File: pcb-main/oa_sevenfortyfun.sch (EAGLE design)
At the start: 46 parts, among them J1 1X01-TERM, J2 1X01-TERM, J3 1X01-TERM, J4 1X01-TERM, J5 1X01-TERM, J6 1X01-TERM, J7 1X01-TERM, J8 1X01-TERM, J9 2X04SHR, Q1 2N3904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

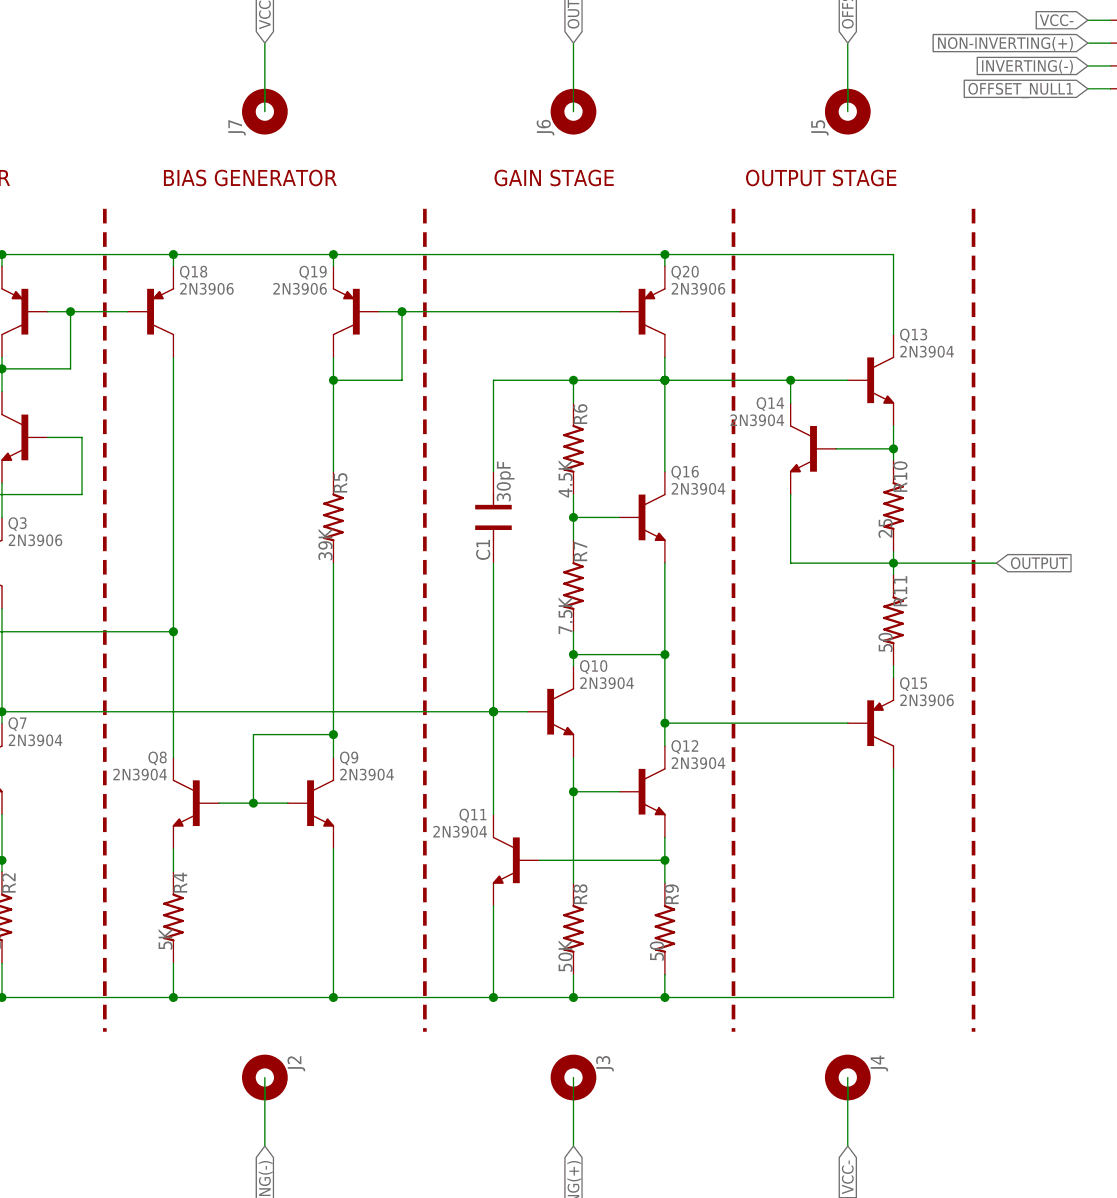
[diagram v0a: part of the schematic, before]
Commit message: matching functional blocks to v1.0
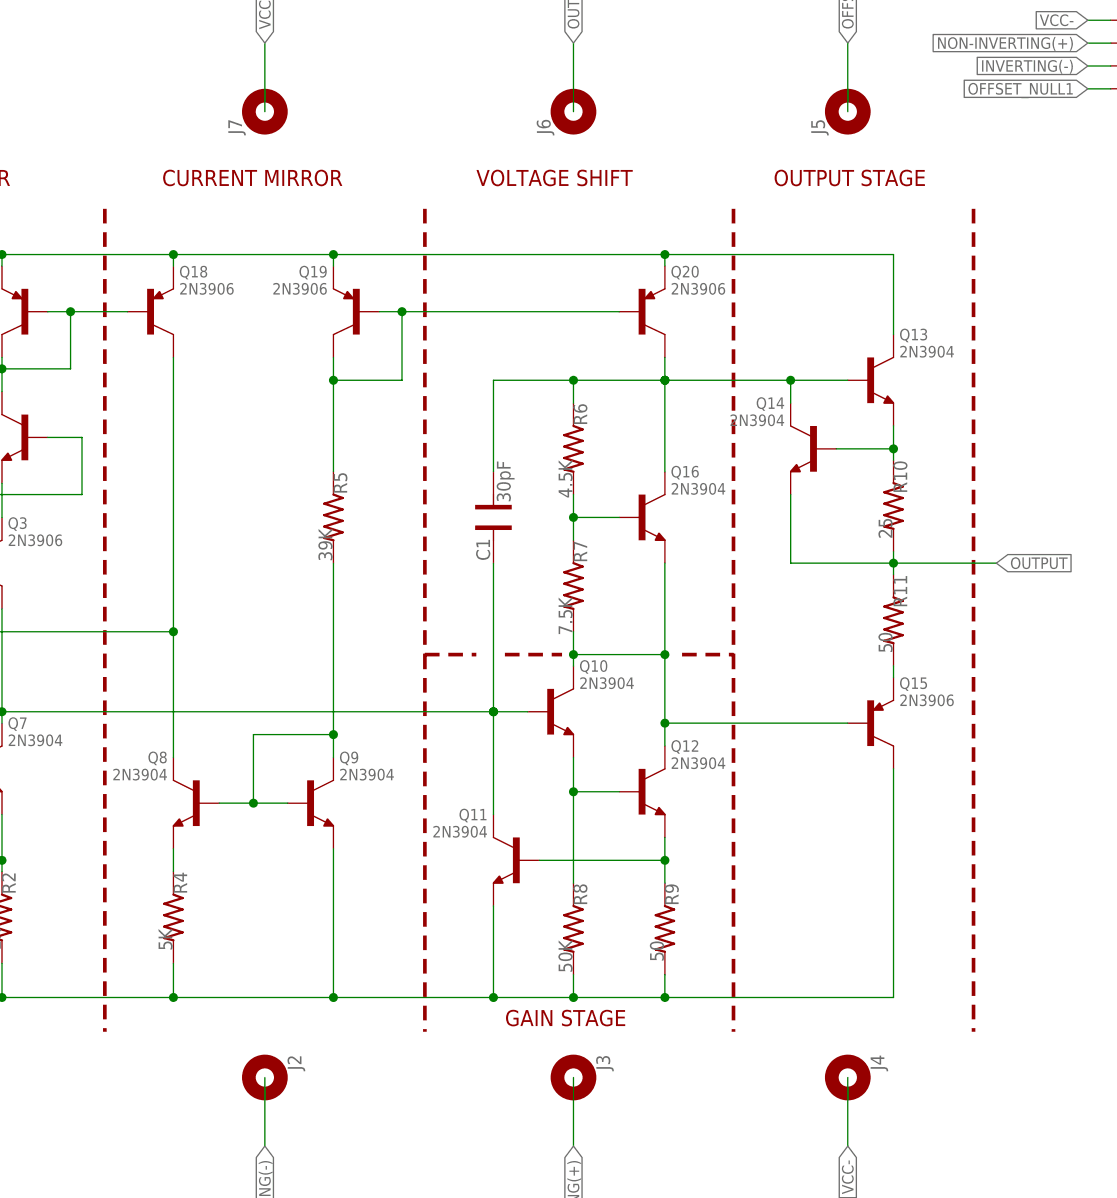
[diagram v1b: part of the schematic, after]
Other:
- note added: "CURRENT MIRROR"
- note added: "VOLTAGE SHIFT"
- note removed: "BIAS GENERATOR"
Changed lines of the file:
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@@
 <plain>
 <wire x1="99.06" y1="147.955" x2="99.06" y2="56.515" width="0.4064" layer="94" style="dashdot"/>
-<wire x1="134.62" y1="147.955" x2="134.62" y2="56.515" width="0.4064" layer="94" style="dashdot"/>
-<wire x1="168.91" y1="147.955" x2="168.91" y2="56.515" width="0.4064" layer="94" style="dashdot"/>
+<wire x1="134.62" y1="147.955" x2="134.62" y2="98.425" width="0.4064" layer="94" style="dashdot"/>
+<wire x1="134.62" y1="98.425" x2="134.62" y2="56.515" width="0.4064" layer="94" style="dashdot"/>
+<wire x1="168.91" y1="147.955" x2="168.91" y2="98.425" width="0.4064" layer="94" style="dashdot"/>
 <text x="60.96" y="150.495" size="1.778" layer="94" font="vector" ratio="15">DIFFERENTIAL AMPLIFIER</text>
-<text x="105.41" y="150.495" size="1.778" layer="94" font="vector" ratio="15">BIAS GENERATOR</text>
-<text x="142.24" y="150.495" size="1.778" layer="94" font="vector" ratio="15">GAIN STAGE</text>
-<text x="170.18" y="150.495" size="1.778" layer="94" font="vector" ratio="15">OUTPUT STAGE</text>
+<text x="105.41" y="150.495" size="1.778" layer="94" font="vector" ratio="15">CURRENT MIRROR</text>
+<text x="140.335" y="150.495" size="1.778" layer="94" font="vector" ratio="15">VOLTAGE SHIFT</text>
+<text x="173.355" y="150.495" size="1.778" layer="94" font="vector" ratio="15">OUTPUT STAGE</text>
+<wire x1="168.91" y1="98.425" x2="168.91" y2="56.515" width="0.4064" layer="94" style="dashdot"/>
 <wire x1="55.88" y1="147.955" x2="55.88" y2="56.515" width="0.4064" layer="94" style="dashdot"/>
 <wire x1="195.58" y1="147.955" x2="195.58" y2="56.515" width="0.4064" layer="94" style="dashdot"/>
@@
 <text x="228.6" y="160.655" size="1.27" layer="94" font="vector" ratio="15">NC</text>
 <text x="76.835" y="166.37" size="1.27" layer="94" font="vector" ratio="15" rot="R90">NOT CONNECTED</text>
+<wire x1="163.195" y1="98.425" x2="168.91" y2="98.425" width="0.4064" layer="94" style="dashdot"/>
+<wire x1="134.62" y1="98.425" x2="140.335" y2="98.425" width="0.4064" layer="94" style="dashdot"/>
+<wire x1="143.51" y1="98.425" x2="149.86" y2="98.425" width="0.4064" layer="94" style="dashdot"/>
+<text x="143.51" y="57.15" size="1.778" layer="94" font="vector" ratio="15">GAIN STAGE</text>
 </plain>
 <instances>

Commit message: updated files
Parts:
- Q1, Q10, Q11, Q12, Q13, Q14, Q16, Q2, Q5, Q6, Q7, Q8, Q9: device Ai_DiscreteSemis:TRANSISTOR-NPN -> Ai_DiscreteSemis:BJT-NPN
- Q15, Q17, Q18, Q19, Q20, Q3, Q4: device Ai_DiscreteSemis:TRANSISTOR-PNP -> Ai_DiscreteSemis:BJT-PNP
- STANDOFF1, STANDOFF2, STANDOFF3, STANDOFF4: value STAND-OFF -> STAND-OFF4; device Ai_Electromechanical:STAND-OFF -> Ai_Electromechanical:STAND-OFF4
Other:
- moved on the sheet: C1, J2, J3, J4, J5, J6, J7, J9, Q10, Q11, Q12, Q13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
